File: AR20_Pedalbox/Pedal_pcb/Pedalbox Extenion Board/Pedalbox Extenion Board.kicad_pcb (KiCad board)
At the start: 2 copper layers, 4 parts, among them P1 MX23A12NF1, U1 ACM_2020, U2 L78L05_SO8, U3 L78L05_SO8

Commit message: Started on PCB layout and added 18pin connector
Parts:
- added C1: 0.33uF, Capacitor_SMD:C_0603_1608Metric, F.Cu at (140.4, 117.7)
- added C2: 0.1uF, Capacitor_SMD:C_0603_1608Metric, F.Cu at (140.4, 128.5)
- added C3: 0.33uF, Capacitor_SMD:C_0603_1608Metric, F.Cu at (148.6, 117.9)
- added C4: 0.1uF, Capacitor_SMD:C_0603_1608Metric, F.Cu at (148.6, 128.6)
- P1: value MX23A12NF1 -> MX23A18NF1; footprint Pedalbox Extenion Board:JAE_MX23A12NF1 -> MX23A18NF1:JAE_MX23A18NF1
- moved P1 83.7 mm to (150.0, 150.0)
- moved U1 56.1 mm to (150.0, 136.0), turned to 180 degrees
- moved U2 53.6 mm to (142.3, 123.2), turned to 90 degrees
- moved U3 42.0 mm to (150.5, 123.2), turned to 90 degrees
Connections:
- net Net-(P1-Pad10) renamed BPS2_Signal
- net Net-(P1-Pad11) renamed BPS1_Signal
- net Net-(P1-Pad8) renamed BPS2_Supply
- net Net-(P1-Pad9) renamed BPS2_GND
- P1 pad 1: Net-(P1-Pad1) -> +12V
- P1 pad 12: Net-(P1-Pad12) -> Steering_Angle_Sensor_Supply
- P1 pad 2: Net-(P1-Pad2) -> APPS1_GND
- P1 pad 3: Net-(P1-Pad3) -> CANH
- P1 pad 4: Net-(P1-Pad4) -> CANL
- P1 pad 5: Net-(P1-Pad5) -> Steering_Angle_Sensor_Supply
- P1 pad 6: Net-(P1-Pad6) -> APPS1_GND
- P1 pad 7: Net-(P1-Pad7) -> Steering_Angle_Sensor_Signal
- U1 pad 1: Net-(U1-Pad1) -> Steering_Angle_Sensor_Signal
- U1 pad 16: GND -> APPS1_GND
- U1 pad 18: GND -> APPS1_GND
- U1 pad 19: GND -> APPS1_GND
- U1 pad 2: Net-(U1-Pad2) -> APPS2_Signal
- U1 pad 21: GND -> APPS1_GND
- U1 pad 24: +5V -> Steering_Angle_Sensor_Supply
- U1 pad 26: Net-(U1-Pad26) -> Steering_Angle_Sensor_Supply
- U1 pad 27: Net-(U1-Pad27) -> CANH
- U1 pad 28: Net-(U1-Pad28) -> Steering_Angle_Sensor_Supply
- U1 pad 29: Net-(U1-Pad29) -> CANL
- U1 pad 3: Net-(U1-Pad3) -> APPS1_Signal
- U1 pad 9: GND -> APPS1_GND
- U2 pad 1: Net-(U2-Pad1) -> APPS1_Supply
- U2 pad 2: Net-(U2-Pad2) -> APPS1_GND
- U2 pad 3: Net-(U2-Pad2) -> APPS1_GND
- U2 pad 6: Net-(U2-Pad2) -> APPS1_GND
- U2 pad 7: Net-(U2-Pad2) -> APPS1_GND
- U2 pad 8: Net-(U2-Pad8) -> +12V
- U3 pad 1: Net-(U3-Pad1) -> APPS2_Supply
- U3 pad 2: Net-(U3-Pad2) -> APPS1_GND
- U3 pad 3: Net-(U3-Pad2) -> APPS1_GND
- U3 pad 6: Net-(U3-Pad2) -> APPS1_GND
- U3 pad 7: Net-(U3-Pad2) -> APPS1_GND
- U3 pad 8: Net-(U3-Pad8) -> +12V
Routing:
- net CANH: track 0.00 -> 18.1 mm
- net CANL: track 0.00 -> 15.3 mm
- net +12V: track 0.00 -> 9.50 mm, vias 0 -> 1
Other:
- board outline added: 52.8 x 45.6 mm

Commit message: Pedalbox PCB Ready - Just need some more silkscreen... ;)
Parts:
- added C5: C_Small, Capacitor_SMD:C_0603_1608Metric_Pad1.05x0.95mm_HandSolder, F.Cu at (149.4, 124.8)
- added C6: C_Small, Capacitor_SMD:C_0603_1608Metric_Pad1.05x0.95mm_HandSolder, F.Cu at (135.1, 129.7)
- added C7: C_Small, Capacitor_SMD:C_0603_1608Metric_Pad1.05x0.95mm_HandSolder, F.Cu at (135.4, 124.8)
- added C8: C_Small, Capacitor_SMD:C_0603_1608Metric_Pad1.05x0.95mm_HandSolder, F.Cu at (149.6, 128.6)
- added C9: C_Small, Capacitor_SMD:C_0603_1608Metric_Pad1.05x0.95mm_HandSolder, F.Cu at (135.2, 135.5)
- added H1: MountingHole, MountingHole:MountingHole_2.2mm_M2, F.Cu at (166.7, 123.2)
- added R1: R_Small, Resistor_SMD:R_0603_1608Metric_Pad1.05x0.95mm_HandSolder, F.Cu at (151.1, 124.8)
- added R10: 4K7, Resistor_SMD:R_0603_1608Metric_Pad1.05x0.95mm_HandSolder, F.Cu at (136.9, 135.5)
- added R2: R_Small, Resistor_SMD:R_0603_1608Metric_Pad1.05x0.95mm_HandSolder, F.Cu at (133.3, 129.8)
- added R3: R_Small, Resistor_SMD:R_0603_1608Metric_Pad1.05x0.95mm_HandSolder, F.Cu at (133.6, 124.7)
- added R4: R_Small, Resistor_SMD:R_0603_1608Metric_Pad1.05x0.95mm_HandSolder, F.Cu at (151.3, 128.6)
- added R5: R_Small, Resistor_SMD:R_0603_1608Metric_Pad1.05x0.95mm_HandSolder, F.Cu at (133.4, 135.5)
- added R6: 4K7, Resistor_SMD:R_0603_1608Metric_Pad1.05x0.95mm_HandSolder, F.Cu at (136.9, 129.8)
- added R7: 4K7, Resistor_SMD:R_0603_1608Metric_Pad1.05x0.95mm_HandSolder, F.Cu at (147.6, 124.7)
- added R8: 4K7, Resistor_SMD:R_0603_1608Metric_Pad1.05x0.95mm_HandSolder, F.Cu at (137.1, 124.8)
- added R9: 4K7, Resistor_SMD:R_0603_1608Metric_Pad1.05x0.95mm_HandSolder, F.Cu at (147.8, 128.6)
- C1, C2, C3, C4: footprint Capacitor_SMD:C_0603_1608Metric -> Capacitor_SMD:C_0603_1608Metric_Pad1.05x0.95mm_HandSolder
- moved C2 23.4 mm to (163.3, 133.7), turned to 90 degrees
- moved C1 21.1 mm to (154.1, 133.8)
- moved U2 18.9 mm to (158.7, 132.7), turned to 180 degrees
- moved C4 14.8 mm to (163.1, 125.7), turned to 90 degrees
- moved C3 9.50 mm to (154.0, 125.7)
- moved U3 8.20 mm to (158.5, 124.7), turned to 180 degrees
- moved U1 8.06 mm to (143.0, 132.0), turned to 90 degrees
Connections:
- C1 pad 2: APPS1_GND -> GND
- C2 pad 2: APPS1_GND -> GND
- C3 pad 2: APPS1_GND -> GND
- C4 pad 2: APPS1_GND -> GND
- P1 pad 1: +12V -> APPS1_Supply
- P1 pad 10: BPS2_Signal -> APPS2_Supply
- P1 pad 11: BPS1_Signal -> GND
- P1 pad 12: Steering_Angle_Sensor_Supply -> GND
- P1 pad 13: APPS2_Supply -> +5V
- P1 pad 14: APPS1_GND -> +5V
- P1 pad 15: APPS2_Signal -> GND
- P1 pad 16: APPS1_Supply -> GND
- P1 pad 17: APPS1_GND -> GND
- P1 pad 18: APPS1_Signal -> GND
- P1 pad 2: APPS1_GND -> APPS1_Signal
- P1 pad 3: CANH -> APPS2_Signal
- P1 pad 4: CANL -> CANH
- P1 pad 5: Steering_Angle_Sensor_Supply -> CANL
- P1 pad 6: APPS1_GND -> +12V
- P1 pad 7: Steering_Angle_Sensor_Signal -> BPS2_Signal
- P1 pad 8: BPS2_Supply -> BPS1_Signal
- P1 pad 9: BPS2_GND -> Steering_Angle_Sensor_Signal
- U1 pad 1: Steering_Angle_Sensor_Signal -> APPS1_Signal_Filtered
- U1 pad 16: APPS1_GND -> GND
- U1 pad 18: APPS1_GND -> GND
- U1 pad 19: APPS1_GND -> GND
- U1 pad 2: APPS2_Signal -> Steering_Angle_Sensor_Signal_Filtered
- U1 pad 21: APPS1_GND -> GND
- U1 pad 24: Steering_Angle_Sensor_Supply -> +5V
- U1 pad 26: Steering_Angle_Sensor_Supply -> +5V
- U1 pad 28: Steering_Angle_Sensor_Supply -> +5V
- U1 pad 3: APPS1_Signal -> APPS2_Signal_Filtered
- U1 pad 4: Net-(U1-Pad4) -> BPS1_Signal_Filtered
- U1 pad 6: Net-(U1-Pad6) -> BPS2_Signal_Filtered
- U1 pad 9: APPS1_GND -> GND
- U2 pad 2: APPS1_GND -> GND
- U2 pad 3: APPS1_GND -> GND
- U2 pad 6: APPS1_GND -> GND
- U2 pad 7: APPS1_GND -> GND
- U3 pad 2: APPS1_GND -> GND
- U3 pad 3: APPS1_GND -> GND
- U3 pad 6: APPS1_GND -> GND
- U3 pad 7: APPS1_GND -> GND
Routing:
- net +5V: track 0.00 -> 33.4 mm, vias 0 -> 1
- net +12V: track 9.50 -> 41.1 mm, vias 1 -> 2
- net APPS2_Supply: track 0.00 -> 30.6 mm
- net Steering_Angle_Sensor_Signal: track 0.00 -> 29.9 mm
- net APPS1_Signal: track 0.00 -> 24.5 mm
- net BPS1_Signal: track 0.00 -> 23.2 mm
- net APPS1_Supply: track 0.00 -> 19.3 mm
- net APPS2_Signal: track 0.00 -> 17.6 mm
- net BPS2_Signal: track 0.00 -> 16.9 mm
- net BPS2_Signal_Filtered: track 0.00 -> 12.5 mm
- net BPS1_Signal_Filtered: track 0.00 -> 8.53 mm
- net Steering_Angle_Sensor_Signal_Filtered: track 0.00 -> 7.81 mm
- net APPS2_Signal_Filtered: track 0.00 -> 6.66 mm
- net APPS1_Signal_Filtered: track 0.00 -> 6.51 mm
- net CANH: track 18.1 -> 12.5 mm
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- added copper zone on B.Cu, net GND
- added copper zone on F.Cu, net GND
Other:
- board size 52.8 x 45.6 mm -> 40.9 x 37.3 mm
- board text added: "APPS1"
- board text added: "APPS2"
- board text added: "Pedalbox Extention board Pedalbox Bachelor Thesis 2020 V. 1.0"

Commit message: Checkout
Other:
- board size 40.9 x 37.3 mm -> 41 x 37.2 mm
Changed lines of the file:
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@@
   (page A4)
   (layers
-    (0 F.Cu signal hide)
-    (31 B.Cu signal)
+    (0 F.Cu signal)
+    (31 B.Cu signal hide)
     (32 B.Adhes user hide)
     (33 F.Adhes user hide)
-    (34 B.Paste user)
-    (35 F.Paste user hide)
-    (36 B.SilkS user)
-    (37 F.SilkS user hide)
-    (38 B.Mask user)
-    (39 F.Mask user hide)
+    (34 B.Paste user hide)
+    (35 F.Paste user)
+    (36 B.SilkS user hide)
+    (37 F.SilkS user)
+    (38 B.Mask user hide)
+    (39 F.Mask user)
     (40 Dwgs.User user hide)
     (41 Cmts.User user hide)
@@
     (44 Edge.Cuts user)
     (45 Margin user hide)
-    (46 B.CrtYd user)
-    (47 F.CrtYd user hide)
-    (48 B.Fab user)
-    (49 F.Fab user hide)
+    (46 B.CrtYd user hide)
+    (47 F.CrtYd user)
+    (48 B.Fab user hide)
+    (49 F.Fab user)
   )
   (setup
-    (last_trace_width 0.508)
+    (last_trace_width 0.25)
     (user_trace_width 0.3048)
     (user_trace_width 0.4064)
@@
     (fp_circle (center 0 0) (end 2.45 0) (layer F.CrtYd) (width 0.05))
     (fp_circle (center 0 0) (end 2.2 0) (layer Cmts.User) (width 0.15))
-    (fp_text user %R (at 0.3 0) (layer F.Fab)
+    (fp_text user %R (at 0.2871 -0.2154) (layer F.Fab)
       (effects (font (size 1 1) (thickness 0.15)))
     )
@@
     (effects (font (size 1.5 1.5) (thickness 0.3)) (justify left mirror))
   )
-  (gr_line (start 128.8415 120.015) (end 128.8415 157.3022) (layer Edge.Cuts) (width 0.1))
-  (gr_line (start 169.7609 120.015) (end 169.7609 157.3022) (layer Edge.Cuts) (width 0.1))
-  (gr_line (start 128.8415 120.015) (end 169.7609 120.015) (layer Edge.Cuts) (width 0.1))
-  (gr_line (start 128.8415 157.3022) (end 169.7609 157.3022) (layer Edge.Cuts) (width 0.1))
-  (via (at 138.9126 134.3914) (size 0.8) (drill 0.4) (layers F.Cu B.Cu) (net 34))
-  (via (at 134.366 132.715) (size 0.8) (drill 0.4) (layers F.Cu B.Cu) (net 34))
-  (via (at 135.4709 138.303) (size 0.8) (drill 0.4) (layers F.Cu B.Cu) (net 34))
-  (via (at 130.175 143.1925) (size 0.8) (drill 0.4) (layers F.Cu B.Cu) (net 34))
-  (via (at 149.3266 137.668) (size 0.8) (drill 0.4) (layers F.Cu B.Cu) (net 34))
-  (via (at 149.2758 134.7216) (size 0.8) (drill 0.4) (layers F.Cu B.Cu) (net 34))
-  (via (at 149.225 132.6261) (size 0.8) (drill 0.4) (layers F.Cu B.Cu) (net 34))
-  (via (at 145.5928 123.0884) (size 0.8) (drill 0.4) (layers F.Cu B.Cu) (net 34))
-  (via (at 142.6972 123.0122) (size 0.8) (drill 0.4) (layers F.Cu B.Cu) (net 34))
-  (via (at 139.7889 123.0503) (size 0.8) (drill 0.4) (layers F.Cu B.Cu) (net 34))
-  (via (at 155.1432 128.1938) (size 0.8) (drill 0.4) (layers F.Cu B.Cu) (net 34))
-  (via (at 163.7665 128.7526) (size 0.8) (drill 0.4) (layers F.Cu B.Cu) (net 34))
-  (via (at 155.4353 137.6172) (size 0.8) (drill 0.4) (layers F.Cu B.Cu) (net 34))
-  (via (at 158.0007 141.3002) (size 0.8) (drill 0.4) (layers F.Cu B.Cu) (net 34))
-  (via (at 161.4424 137.541) (size 0.8) (drill 0.4) (layers F.Cu B.Cu) (net 34))
-  (via (at 132.2451 127.1778) (size 0.8) (drill 0.4) (layers F.Cu B.Cu) (net 34))
+  (gr_line (start 129 120) (end 129 157.2) (layer Edge.Cuts) (width 0.1))
+  (gr_line (start 170 120) (end 170 157.2) (layer Edge.Cuts) (width 0.1))
+  (gr_line (start 129 120) (end 170 120) (layer Edge.Cuts) (width 0.1))
+  (gr_line (start 129 157.2) (end 170 157.2) (layer Edge.Cuts) (width 0.1))
   (segment (start 140.53 137.473) (end 139.9794 138.0236) (width 0.508) (layer F.Cu) (net 1))
   (segment (start 141.1 137.473) (end 140.53 137.473) (width 0.508) (layer F.Cu) (net 1))
@@
   (segment (start 151.1173 123.9025) (end 151.5758 123.9025) (width 0.508) (layer F.Cu) (net 20))
   (segment (start 151.5758 123.9025) (end 152.5016 124.8283) (width 0.508) (layer F.Cu) (net 20))
-  (via (at 129.4257 132.2324) (size 0.8) (drill 0.4) (layers F.Cu B.Cu) (net 34))
   (segment (start 164.4256 134.6187) (end 163.2712 134.6187) (width 0.508) (layer F.Cu) (net 21))
   (segment (start 166.37 136.5631) (end 164.4256 134.6187) (width 0.508) (layer F.Cu) (net 21))
@@
   (segment (start 139.2555 128.858178) (end 139.2555 131.0005) (width 0.508) (layer F.Cu) (net 33))
   (segment (start 139.2555 131.0005) (end 136.8552 133.4008) (width 0.508) (layer F.Cu) (net 33))
+  (via (at 138.9126 134.3914) (size 0.8) (drill 0.4) (layers F.Cu B.Cu) (net 34))
+  (via (at 134.366 132.715) (size 0.8) (drill 0.4) (layers F.Cu B.Cu) (net 34))
+  (via (at 135.4709 138.303) (size 0.8) (drill 0.4) (layers F.Cu B.Cu) (net 34))
+  (via (at 130.175 143.1925) (size 0.8) (drill 0.4) (layers F.Cu B.Cu) (net 34))
+  (via (at 149.3266 137.668) (size 0.8) (drill 0.4) (layers F.Cu B.Cu) (net 34))
+  (via (at 149.2758 134.7216) (size 0.8) (drill 0.4) (layers F.Cu B.Cu) (net 34))
+  (via (at 149.225 132.6261) (size 0.8) (drill 0.4) (layers F.Cu B.Cu) (net 34))
+  (via (at 145.5928 123.0884) (size 0.8) (drill 0.4) (layers F.Cu B.Cu) (net 34))
+  (via (at 142.6972 123.0122) (size 0.8) (drill 0.4) (layers F.Cu B.Cu) (net 34))
+  (via (at 139.7889 123.0503) (size 0.8) (drill 0.4) (layers F.Cu B.Cu) (net 34))
+  (via (at 155.1432 128.1938) (size 0.8) (drill 0.4) (layers F.Cu B.Cu) (net 34))
+  (via (at 163.7665 128.7526) (size 0.8) (drill 0.4) (layers F.Cu B.Cu) (net 34))
+  (via (at 155.4353 137.6172) (size 0.8) (drill 0.4) (layers F.Cu B.Cu) (net 34))
+  (via (at 158.0007 141.3002) (size 0.8) (drill 0.4) (layers F.Cu B.Cu) (net 34))
+  (via (at 161.4424 137.541) (size 0.8) (drill 0.4) (layers F.Cu B.Cu) (net 34))
+  (via (at 132.2451 127.1778) (size 0.8) (drill 0.4) (layers F.Cu B.Cu) (net 34))
+  (via (at 130.5687 124.0028) (size 0.8) (drill 0.4) (layers F.Cu B.Cu) (net 34))
   (via (at 139.3063 140.8303) (size 0.8) (drill 0.4) (layers F.Cu B.Cu) (net 34))
   (segment (start 150 149.666726) (end 148.892326 150.7744) (width 0.508) (layer B.Cu) (net 35))

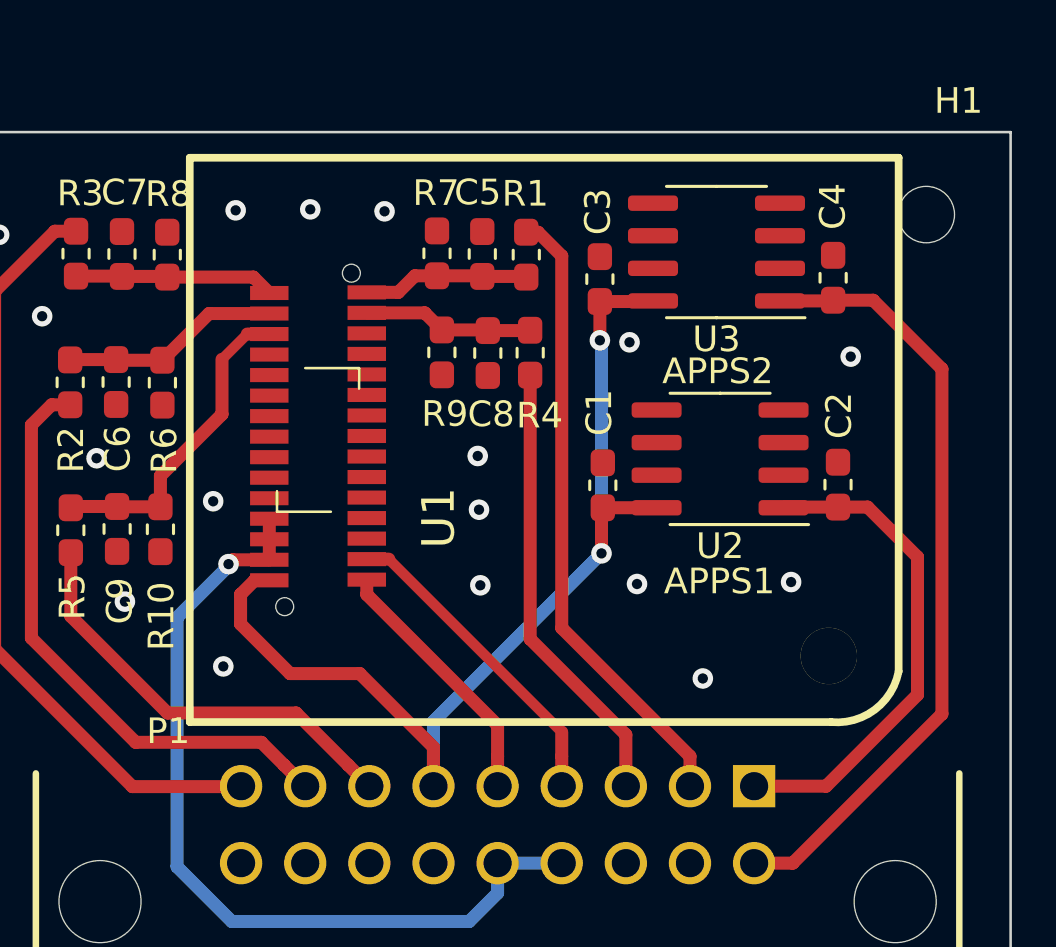
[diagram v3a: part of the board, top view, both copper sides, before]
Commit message: Fixed traces, changed ACM footprint and generated gerber
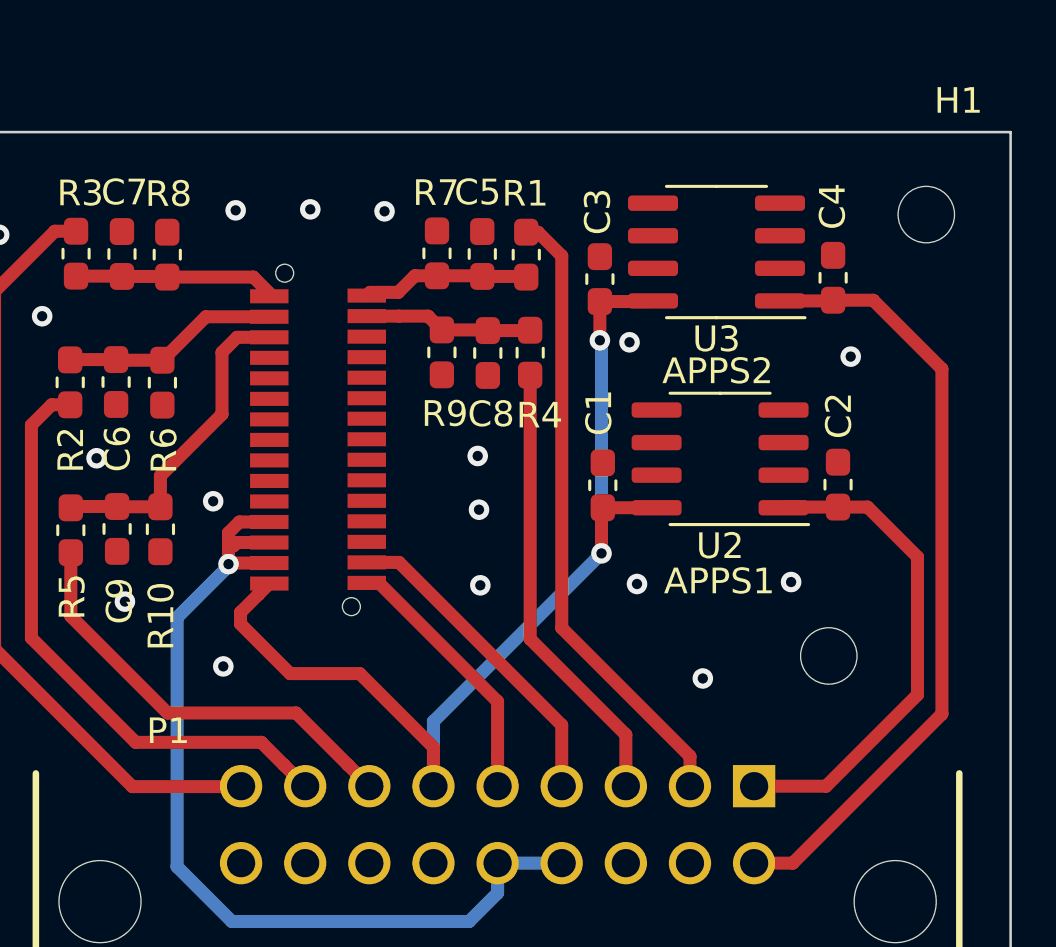
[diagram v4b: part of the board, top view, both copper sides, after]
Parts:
- U1: footprint Pedalbox Extenion Board:ACM_2020_Footprint -> Pedalbox Extenion Board:ACM_2020_Footprint_wo_silk
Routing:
- net +5V: track 33.4 -> 36.4 mm
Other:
- rule trace_min: 0.2 -> 0.128
